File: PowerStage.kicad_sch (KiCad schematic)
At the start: 18 parts, among them U2 LMR14020

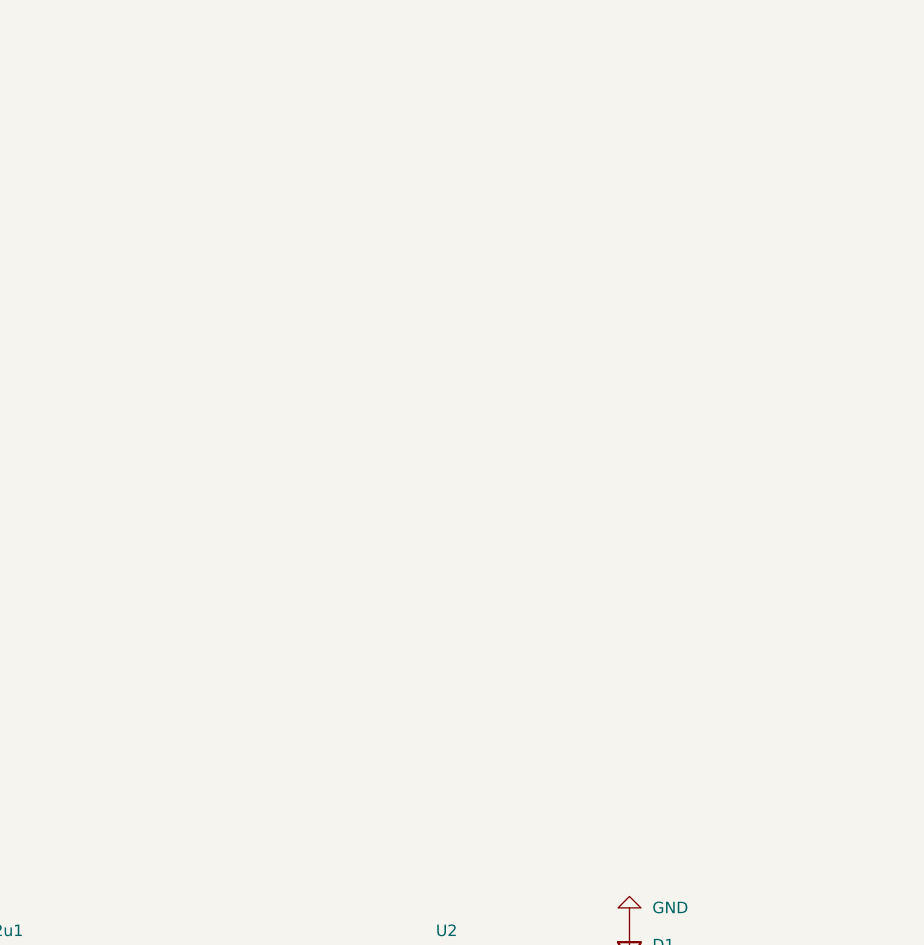
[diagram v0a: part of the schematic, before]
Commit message: 5v supplies added
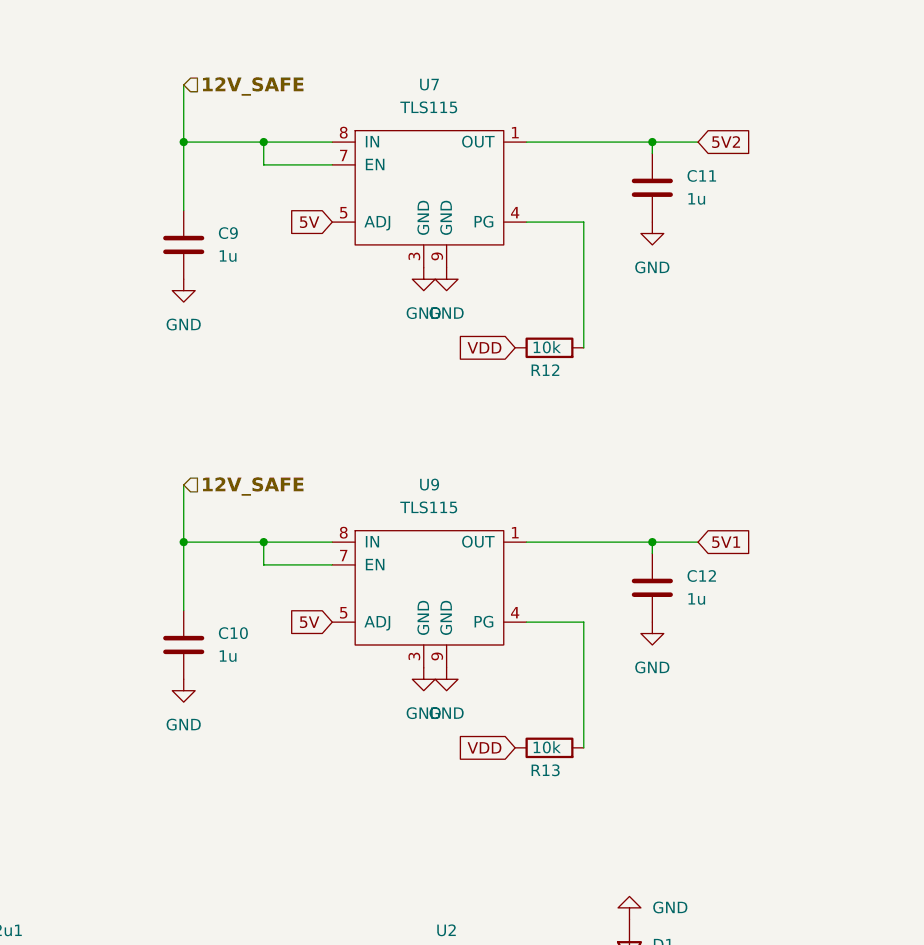
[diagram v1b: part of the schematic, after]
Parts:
- added C10, C11, C12, C9: 1u, Capacitor_SMD:C_0603_1608Metric, symbol Device:C
- added R12, R13: 10k, Resistor_SMD:R_0402_1005Metric, symbol Device:R
- added U7, U9: TLS115, Package_SO:Infineon_PG-DSO-8-27_3.9x4.9mm_EP2.65x3mm_ThermalVias, symbol Simon:TLS115
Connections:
- net 12V_SAFE: now also C10.1, C9.1, U7.7 (EN), U7.8 (IN), U9.7 (EN), U9.8 (IN)
- net 5V: now also U7.5 (ADJ), U9.5 (ADJ)
- net GND: now also C10.2, C11.2, C12.2, C9.2, U7.3 (GND), U7.9 (GND), U9.3 (GND), U9.9 (GND)
- new net: R13.2, U9.4 (PG)
- new net: R12.2, U7.4 (PG)
- new net 5V1: C12.1, U9.1 (OUT)
- new net 5V2: C11.1, U7.1 (OUT)
- new net VDD: R12.1, R13.1
